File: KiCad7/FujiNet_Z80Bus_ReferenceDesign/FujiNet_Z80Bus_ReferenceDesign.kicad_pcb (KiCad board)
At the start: 2 copper layers, 180 x 120 mm, 56 parts, among them IC1 74HC32N, IC2 74HC590N, IC3 74HC590N, J8 DIAG-HOST_SYSTEM_BUS, J9 Logic core connector

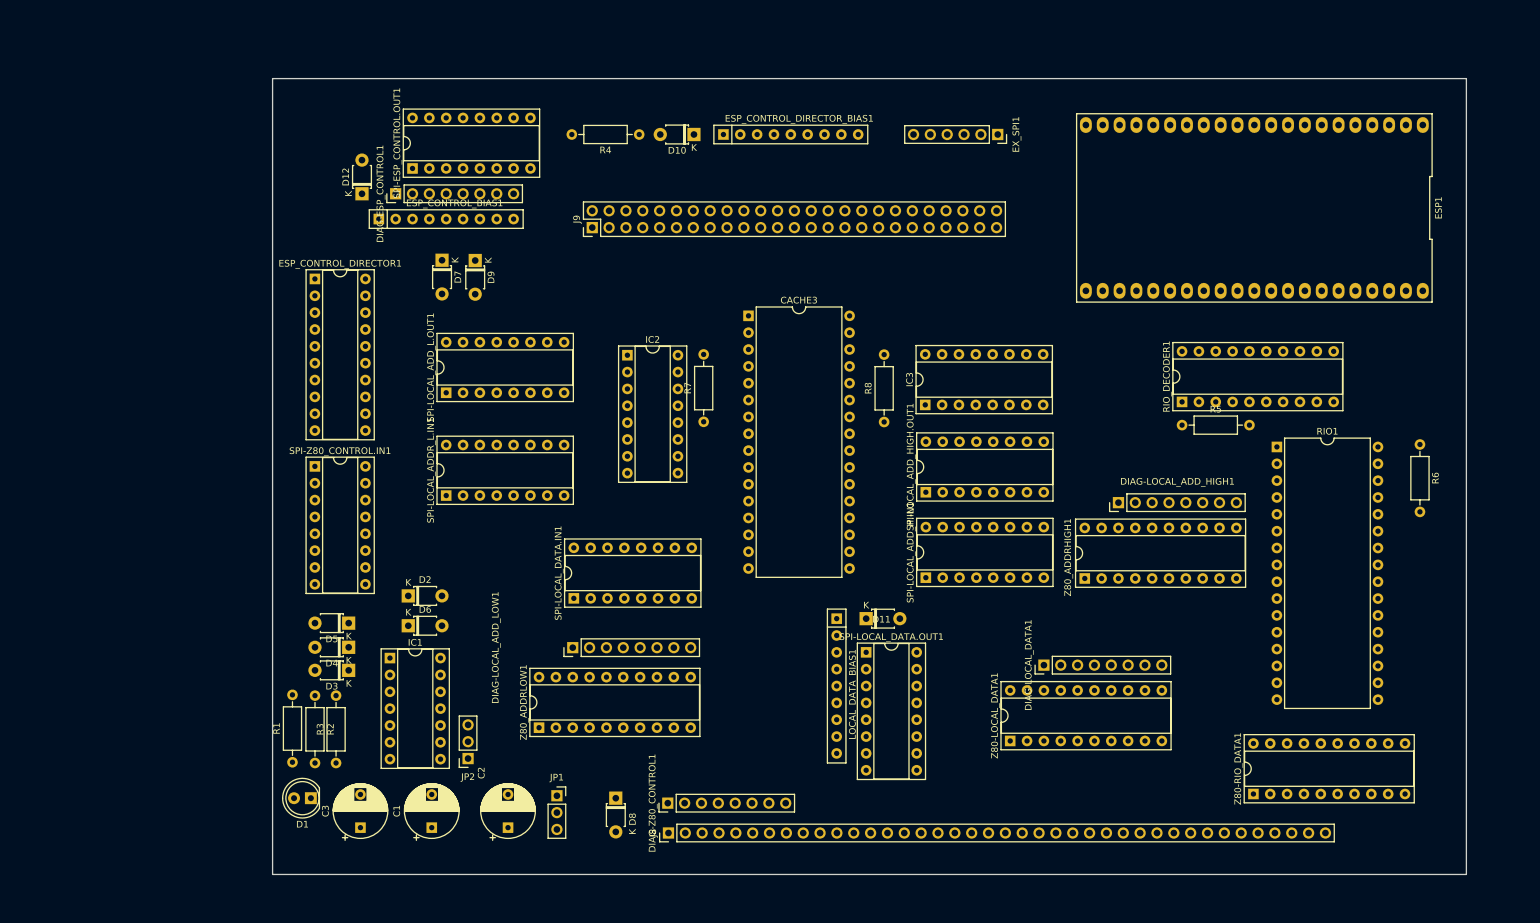
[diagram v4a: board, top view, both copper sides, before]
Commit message: KiCad - Refactoring RIO IOCACHE to projects
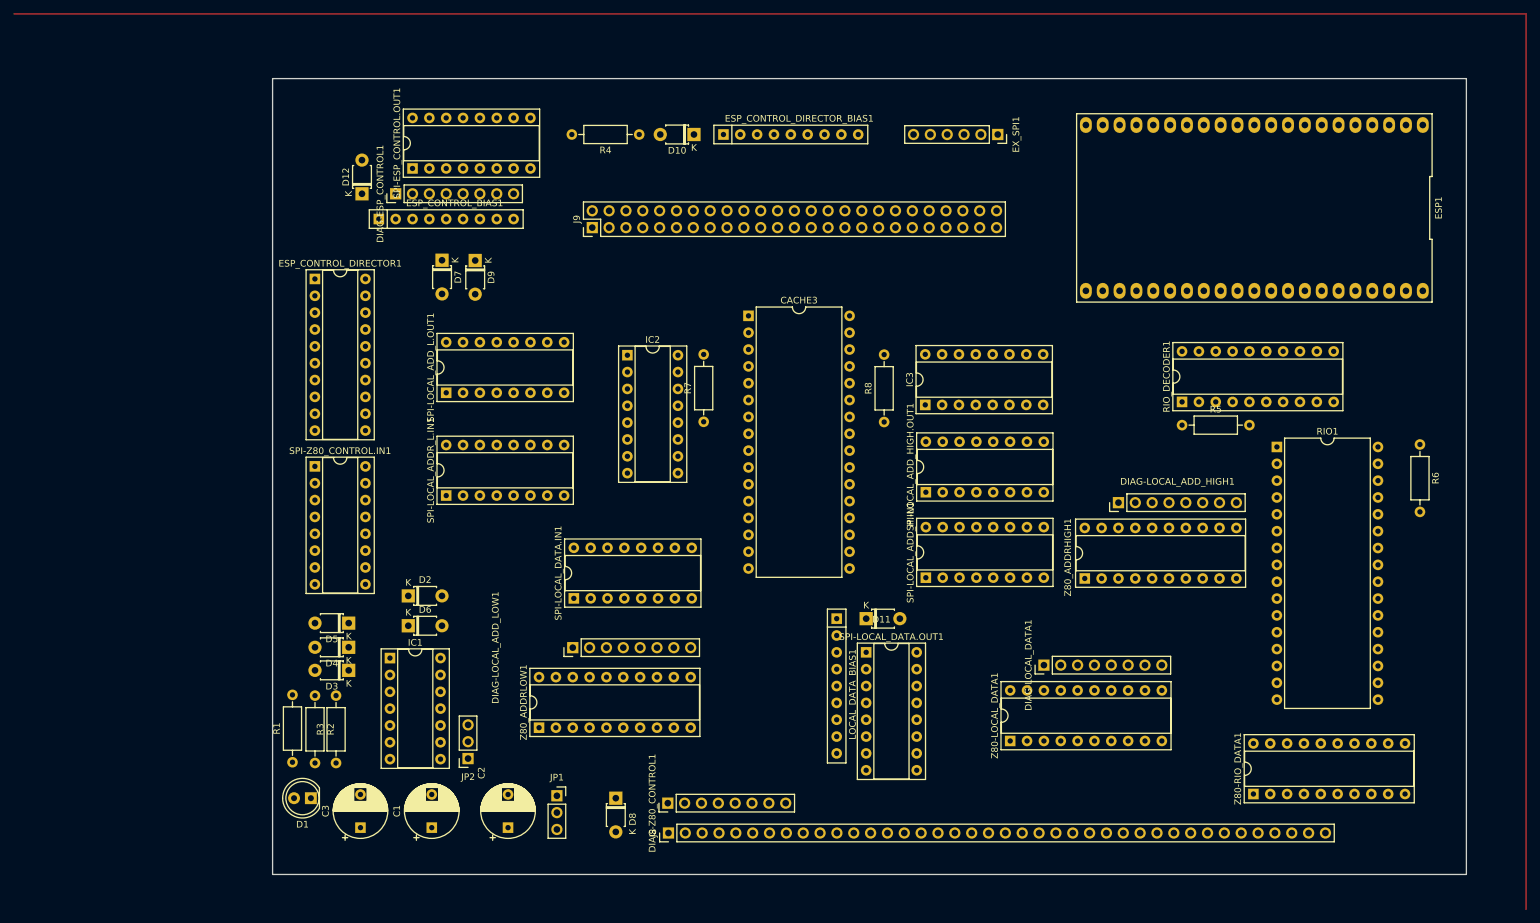
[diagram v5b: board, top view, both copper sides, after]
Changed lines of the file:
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@@
     )
   )
+  (gr_line (start 264 30) (end 36 30)
+    (stroke (width 0.2) (type default)) (layer "F.Cu"))
+  (gr_line (start 264 30) (end 264 165)
+    (stroke (width 0.2) (type default)) (layer "F.Cu"))
   (gr_rect (start 75 39.75) (end 255 159.75)
     (stroke (width 0.05) (type default)) (fill none) (layer "Edge.Cuts"))
@@
   )
   (dimension (type aligned) (layer "F.Cu")
-    (pts (xy 255 39.75) (xy 255 159.75))
+    (pts (xy 264 30) (xy 264 160))
     (height -20.32)
-    (gr_text "120.0000 mm" (at 273.52 99.75 90) (layer "F.Cu")
+    (gr_text "130.0000 mm" (at 282.52 95 90) (layer "F.Cu")
       (effects (font (size 1.5 1.5) (thickness 0.3)))
     )
@@
   )
   (dimension (type aligned) (layer "F.Cu")
-    (pts (xy 264 30) (xy 61 30))
+    (pts (xy 264 30) (xy 64 30))
     (height 12.3952)
-    (gr_text "203.0000 mm" (at 162.5 15.8048) (layer "F.Cu")
+    (gr_text "200.0000 mm" (at 164 15.8048) (layer "F.Cu")
       (effects (font (size 1.5 1.5) (thickness 0.3)))
     )

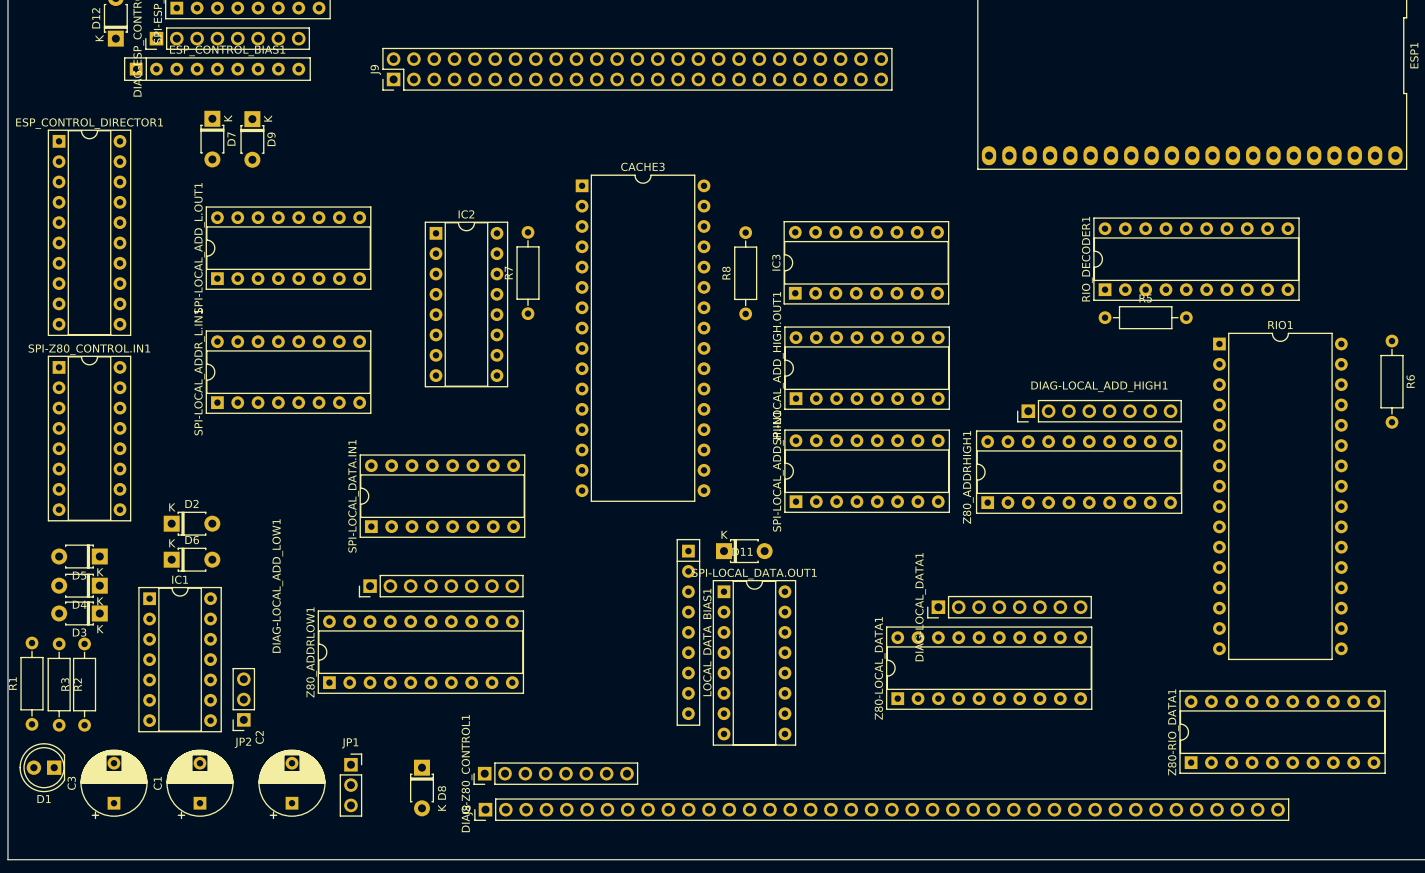
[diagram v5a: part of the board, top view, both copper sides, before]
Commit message: KiCad - Refactored Logic core to GLUE
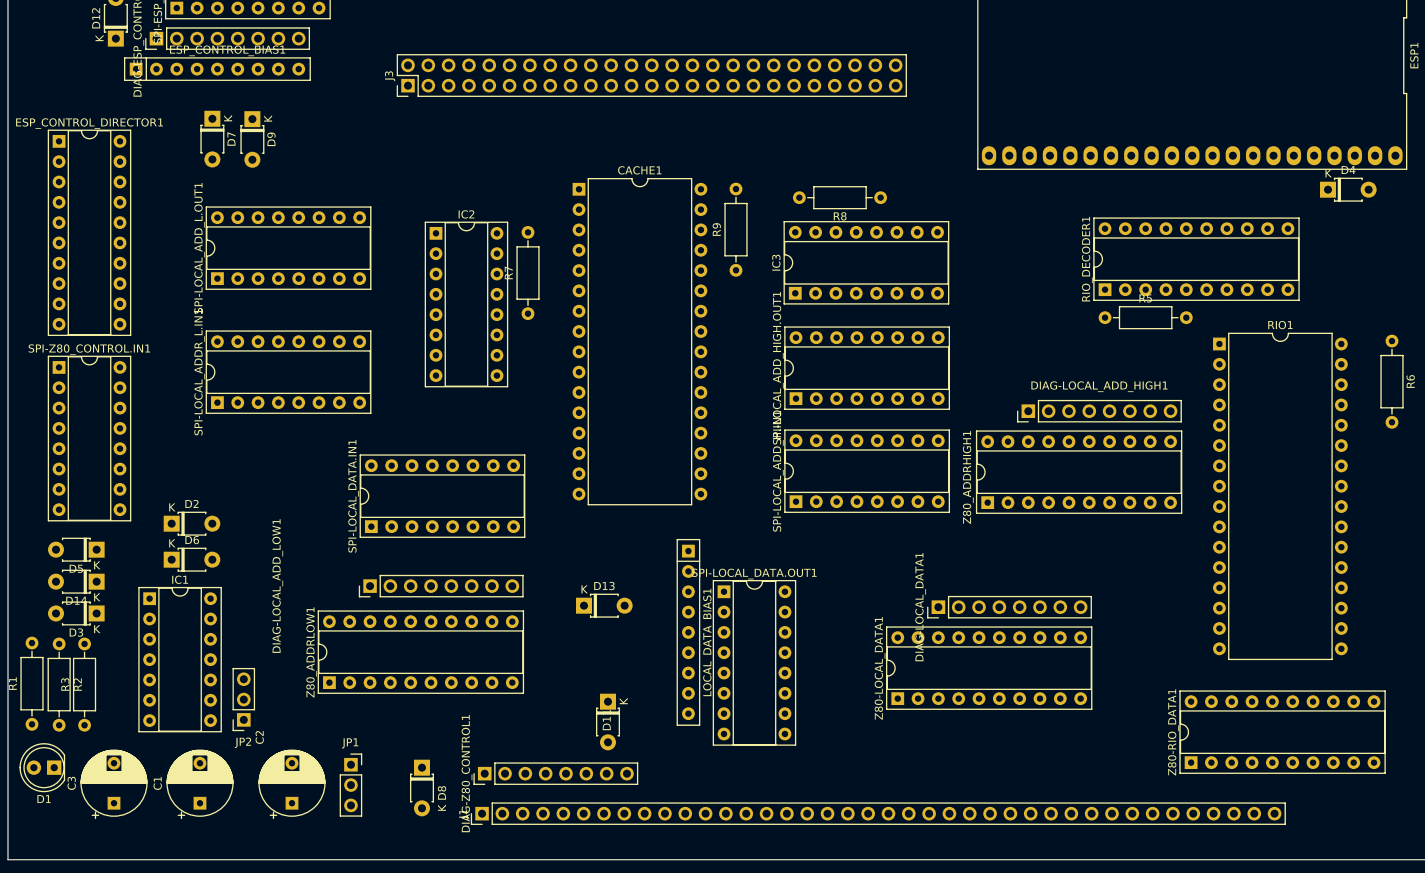
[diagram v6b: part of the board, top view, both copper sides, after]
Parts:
- removed CACHE3: AS6C1008-55PCN, Package_DIP:DIP-32_W15.24mm
- removed J8: DIAG-HOST_SYSTEM_BUS, Connector_PinHeader_2.54mm:PinHeader_1x40_P2.54mm_Vertical
- removed J9: Logic core connector, Connector_PinHeader_2.54mm:PinHeader_2x25_P2.54mm_Vertical
- added CACHE1: AS6C1008-55PCN, Package_DIP:DIP-32_W15.24mm, F.Cu at (146.4, 76.0)
- added D13: 1N4148, Diode_THT:D_T-1_P5.08mm_Horizontal, F.Cu at (147.0, 128.0)
- added D14: 1N4148, Diode_THT:D_T-1_P5.08mm_Horizontal, F.Cu at (86.1, 125.0)
- added J1: DIAG-HOST_SYSTEM_BUS, Connector_PinHeader_2.54mm:PinHeader_1x40_P2.54mm_Vertical, F.Cu at (134.3, 154.0)
- added J3: Logic core connector, Connector_PinHeader_2.54mm:PinHeader_2x25_P2.54mm_Vertical, F.Cu at (125.0, 63.0)
- added R9: 10K, Resistor_THT:R_Axial_DIN0207_L6.3mm_D2.5mm_P10.16mm_Horizontal, F.Cu at (166.0, 86.1)
- R2: value 22K -> R10K
- R5: value 10K -> 22K
- moved D4 161.3 mm to (240.0, 76.0), turned to 0 degrees
- moved D11 23.8 mm to (150.0, 140.0), turned to -90 degrees
- moved R8 22.3 mm to (184.1, 77.0), turned to 180 degrees
- moved D5 0.94 mm to (86.1, 121.0)
- moved D3 0.39 mm to (86.1, 129.0)
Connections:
- net /CORE/ESP_CONTROL.WR+ESP_PULSE renamed /CORE_ESP32-WROVER/ESP_CONTROL.WR+ESP_PULSE
- net /CORE/ESP_SPI_INT.CE renamed /CORE_ESP32-WROVER/ESP_SPI_INT.CE
- net /CORE/ESP_SPI_INT.MISO renamed /CORE_ESP32-WROVER/ESP_SPI_INT.MISO
- net /CORE/ESP_SPI_INT.MOSI renamed /CORE_ESP32-WROVER/ESP_SPI_INT.MOSI
- net /CORE/ESP_SPI_INT.OE renamed /CORE_ESP32-WROVER/ESP_SPI_INT.OE
- net /CORE/ESP_SPI_INT.PL renamed /CORE_ESP32-WROVER/ESP_SPI_INT.PL
- net /CORE/ESP_SPI_INT.SCK renamed /CORE_ESP32-WROVER/ESP_SPI_INT.SCK
- net /CORE/ESP_SPI_INT.STC renamed /CORE_ESP32-WROVER/ESP_SPI_INT.STC
- net /CORE/EX_MISO renamed /CORE_ESP32-WROVER/EX_MISO
- net /CORE/EX_MOSI renamed /CORE_ESP32-WROVER/EX_MOSI
- net /CORE/EX_SCK renamed /CORE_ESP32-WROVER/EX_SCK
- net /CORE/EX_SS renamed /CORE_ESP32-WROVER/EX_SS
- net /CORE/SD_CARD_SS renamed /CORE_ESP32-WROVER/SD_CARD_SS
- net /RIO/RIO_CE2 renamed /RIO-128K_ZXspectrum/RIO_CE2
- net /RIO/ROM_D0 renamed /RIO-128K_ZXspectrum/ROM_D0
- net /RIO/ROM_D1 renamed /RIO-128K_ZXspectrum/ROM_D1
- net /RIO/ROM_D2 renamed /RIO-128K_ZXspectrum/ROM_D2
- net /RIO/ROM_D3 renamed /RIO-128K_ZXspectrum/ROM_D3
- net /RIO/ROM_D4 renamed /RIO-128K_ZXspectrum/ROM_D4
- net /RIO/ROM_D5 renamed /RIO-128K_ZXspectrum/ROM_D5
- net /RIO/ROM_D6 renamed /RIO-128K_ZXspectrum/ROM_D6
- net /RIO/ROM_D7 renamed /RIO-128K_ZXspectrum/ROM_D7
- C1 pad 1: Net-(D1-K) -> +5V
- C2 pad 1: Net-(D1-K) -> +5V
- C3 pad 1: Net-(D1-K) -> +5V
- D1 pad 1: Net-(D1-K) -> GND
- D10 pad 1: Net-(D10-K) -> /ESP_CONTROL.ROMCS
- D10 pad 2: +5V -> /Z80_CONTROL.ROMCS
- D11 pad 1: Net-(D11-K) -> /ESP_CONTROL.NMI
- D11 pad 2: +5V -> /Z80_CONTROL.NMI
- D2 pad 2: /Z80_CONTROL.RESET -> /CORE_ESP32-WROVER/ESP_PULSE
- D3 pad 1: /Z80_CONTROL.WAIT -> Net-(D2-K)
- D3 pad 2: /CORE/ESP_INT -> /ESP_CONTROL.WR
- D4 pad 1: /Z80_HARDLOCK_RESET -> Net-(D4-K)
- D4 pad 2: /CORE/ESP_INT -> /Z80_CONTROL.RESET
- D5 pad 1: /Z80_CONTROL.BUSACK -> /Z80_CONTROL.WAIT
- D5 pad 2: /CORE/ESP_INT -> /CORE_ESP32-WROVER/ESP_INT
- D6 pad 1: /ESP_CONTROL.BUSRQ -> /Z80_HARDLOCK_RESET
- D6 pad 2: /Z80_CONTROL.BUSRQ -> /CORE_ESP32-WROVER/ESP_INT
- D7 pad 1: /ESP_CONTROL.WAIT -> /Z80_CONTROL.BUSACK
- D7 pad 2: /Z80_CONTROL.WAIT -> /CORE_ESP32-WROVER/ESP_INT
- D8 pad 1: /ESP_CONTROL.ROMCS -> /ESP_CONTROL.BUSRQ
- D8 pad 2: /Z80_CONTROL.ROMCS -> /Z80_CONTROL.BUSRQ
- D9 pad 1: /ESP_CONTROL.NMI -> /ESP_CONTROL.WAIT
- D9 pad 2: /Z80_CONTROL.NMI -> /Z80_CONTROL.WAIT
- ESP1 pad 11: /CORE/ESP_PULSE -> /CORE_ESP32-WROVER/ESP_PULSE
- ESP1 pad 3: /CORE/ESP_INT -> /CORE_ESP32-WROVER/ESP_INT
- ESP1 pad 35: Net-(D2-K) -> Net-(D4-K)
- ESP_CONTROL_BIAS1 pad 1: Net-(D12-K) -> Net-(D14-K)
- ESP_CONTROL_DIRECTOR_BIAS1 pad 1: Net-(D10-K) -> Net-(D12-K)
- IC1 pad 12: /CORE/ESP_PULSE -> /CORE_ESP32-WROVER/ESP_PULSE
- JP1 pad 3: Net-(D1-K) -> Net-(D_PSUsafety1-K)
- LOCAL_DATA_BIAS1 pad 1: Net-(D11-K) -> Net-(D13-K)
- R1 pad 1: Net-(D1-A) -> +5V
- R1 pad 2: +5V -> Net-(D1-A)
- R2 pad 1: /CORE/ESP_INT -> Net-(D2-K)
- R2 pad 2: +5V -> GND
- R3 pad 1: GND -> /CORE_ESP32-WROVER/ESP_INT
- R3 pad 2: /CORE/ESP_INT -> +5V
- R4 pad 1: +5V -> GND
- R4 pad 2: /CORE/ESP_SPI_INT.MR -> /CORE_ESP32-WROVER/ESP_INT
- R5 pad 1: Net-(RIO_DECODER1-A->B) -> +5V
- R5 pad 2: +5V -> /CORE_ESP32-WROVER/ESP_SPI_INT.MR
- R7 pad 1: /CACHE_DATASTATUS -> Net-(RIO_DECODER1-A->B)
- R8 pad 1: /CACHE/CACHE_CE2 -> /CACHE_DATASTATUS
- SPI-ESP_CONTROL.OUT1 pad 10: /CORE/ESP_SPI_INT.MR -> /CORE_ESP32-WROVER/ESP_SPI_INT.MR
- SPI-LOCAL_ADD_HIGH.OUT1 pad 10: /CORE/ESP_SPI_INT.MR -> /CORE_ESP32-WROVER/ESP_SPI_INT.MR
- SPI-LOCAL_ADD_L.OUT1 pad 10: /CORE/ESP_SPI_INT.MR -> /CORE_ESP32-WROVER/ESP_SPI_INT.MR
- SPI-LOCAL_DATA.OUT1 pad 10: /CORE/ESP_SPI_INT.MR -> /CORE_ESP32-WROVER/ESP_SPI_INT.MR
